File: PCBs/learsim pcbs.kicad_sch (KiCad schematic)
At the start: 54 parts, among them SW1 MHz, SW2 KHz, SW3 2MS1T1B1M2QES-5, U1 ESP32-C6-DEV-KIT-N8, U2 MAX7219, U3 MAX7219

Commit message: Refactor code structure for improved readability and maintainability
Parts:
- removed SW3: 2MS1T1B1M2QES-5, Rotary:SW-TH_2MS1T1B1M2QES-5, symbol Rotary:2MS1T1B1M2QES-5
- added SW4: 2MD1T1B1M2QES-5, Rotary:SW-TH_2MD1T1B1M2QES-5, symbol Rotary:2MD1T1B1M2QES-5
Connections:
- net GND: now also SW4.2
- net LED_12: now also D1.2 (DIN), D5.4 (DOUT); no longer D1.4 (DOUT), D2.2 (DIN)
- net LED_23: now also D1.4 (DOUT), D2.2 (DIN); no longer D2.4 (DOUT), D3.2 (DIN)
- net LED_34: now also D2.4 (DOUT), D3.2 (DIN); no longer D3.4 (DOUT), D4.2 (DIN)
- net LED_45: now also D3.4 (DOUT), D4.2 (DIN); no longer D4.4 (DOUT), D5.2 (DIN)
- net LED_56: now also D4.4 (DOUT); no longer D5.4 (DOUT)
- net LED_DIN: now also D5.2 (DIN); no longer D1.2 (DIN)
- net SW3_A: now also SW4.1; no longer U1.8 (GPIO14)
- net SW3_B: now also SW4.3; no longer U1.15 (EXIO7)
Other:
- moved on the sheet: C6, D1, D2, D3, D4

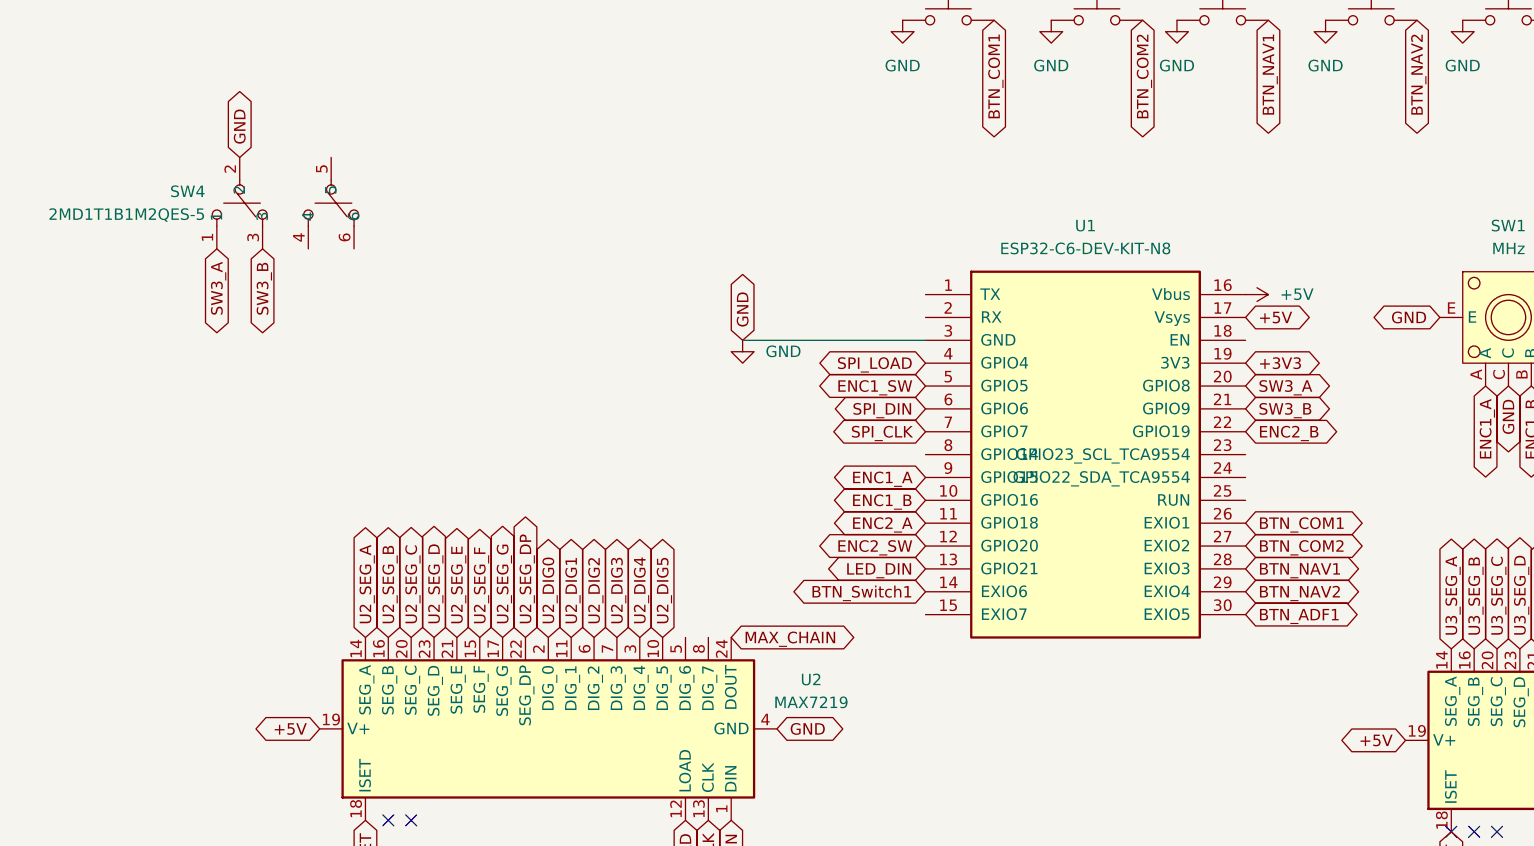
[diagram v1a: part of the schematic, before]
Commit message: Update drill files and job configuration with new timestamps and adjustments
- Updated creation dates in NPTH and PTH drill files to 2026-07-26.
- Adjusted coordinates for several drill points in NPTH file for improved accuracy.
- Modified drill sizes in PTH file, changing T2 from 0.700 to 0.650.
- Added new coordinates in PTH file for additional drill points.
- Updated creation date in job configuration file to 2026-07-26.
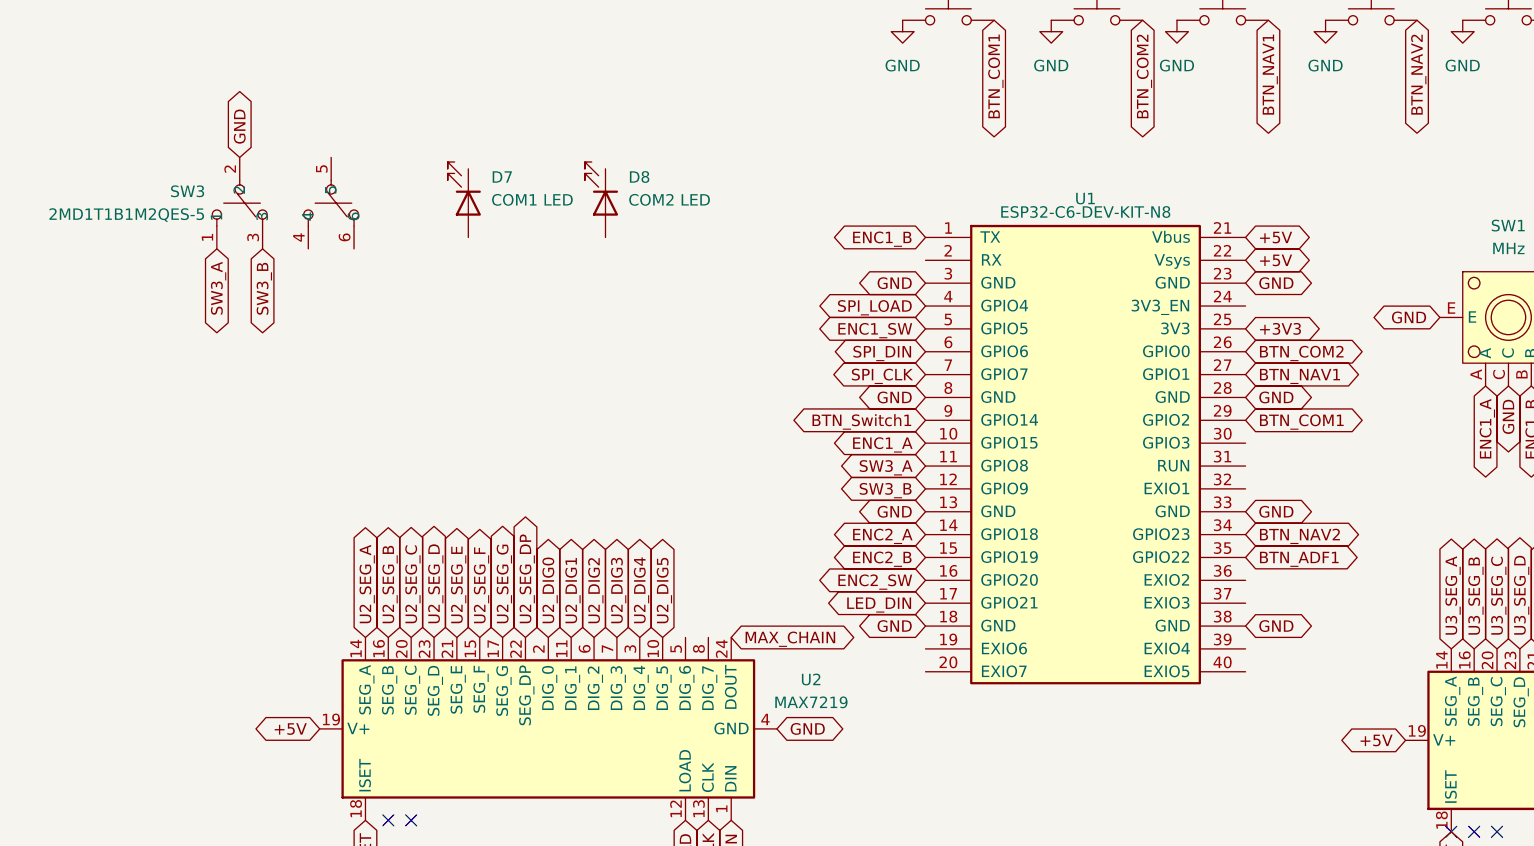
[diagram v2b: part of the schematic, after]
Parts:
- added D7: COM1 LED, LED_THT:LED_D3.0mm, symbol Device:LED
- added D8: COM2 LED, LED_THT:LED_D3.0mm, symbol Device:LED
- renumbered SW4 to SW3
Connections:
- net +3V3: now also U1.25 (3V3); no longer U1.19 (3V3)
- net +5V: now also U1.21 (Vbus), U1.22 (Vsys); no longer U1.16 (Vbus), U1.17 (Vsys)
- net BTN_ADF1: now also U1.35 (GPIO22); no longer U1.30 (EXIO5)
- net BTN_COM1: now also U1.29 (GPIO2); no longer U1.26 (EXIO1)
- net BTN_COM2: now also U1.26 (GPIO0); no longer U1.27 (EXIO2)
- net BTN_NAV1: now also U1.27 (GPIO1); no longer U1.28 (EXIO3)
- net BTN_NAV2: now also U1.34 (GPIO23); no longer U1.29 (EXIO4)
- net BTN_Switch1: now also U1.9 (GPIO14); no longer U1.14 (EXIO6)
- net ENC1_A: now also U1.10 (GPIO15); no longer U1.9 (GPIO15)
- net ENC1_B: now also U1.1 (TX); no longer U1.10 (GPIO16)
- net ENC2_A: now also U1.14 (GPIO18); no longer U1.11 (GPIO18)
- net ENC2_B: now also U1.15 (GPIO19); no longer U1.22 (GPIO19)
- net ENC2_SW: now also U1.16 (GPIO20); no longer U1.12 (GPIO20)
- net GND: now also U1.13 (GND), U1.18 (GND), U1.23 (GND), U1.28 (GND), U1.33 (GND), U1.38 (GND), U1.8 (GND)
- net LED_DIN: now also U1.17 (GPIO21); no longer U1.13 (GPIO21)
- net SW3_A: now also U1.11 (GPIO8); no longer U1.20 (GPIO8)
- net SW3_B: now also U1.12 (GPIO9); no longer U1.21 (GPIO9)

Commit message: Update drill files and job configuration with new creation timestamps and modified drill sizes
- Updated creation timestamps in NPTH and PTH drill files to 2026-07-26T23:00:48.
- Adjusted drill sizes for T4, T5, and T6 in the PTH drill file.
- Added new coordinates in the PTH drill file for improved component placement.
- Updated creation date in the job configuration file to 2026-07-26T23:00:53.
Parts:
- added R17: 150, Resistor_THT:R_Axial_DIN0207_L6.3mm_D2.5mm_P7.62mm_Horizontal, symbol Device:R
- added R18: 470, Resistor_THT:R_Axial_DIN0207_L6.3mm_D2.5mm_P7.62mm_Horizontal, symbol Device:R
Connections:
- net GND: now also D7.1 (K), D8.1 (K)
- net COM2_LED: now reaches U1.2 (RX)
- net COM2_LED: now also R18.2
- net COM1_LED: now reaches U1.30 (GPIO3)
- net COM1_LED: now also R17.2
- net at D8.2 (A): now also R18.1
- net at D7.2 (A): now also R17.1

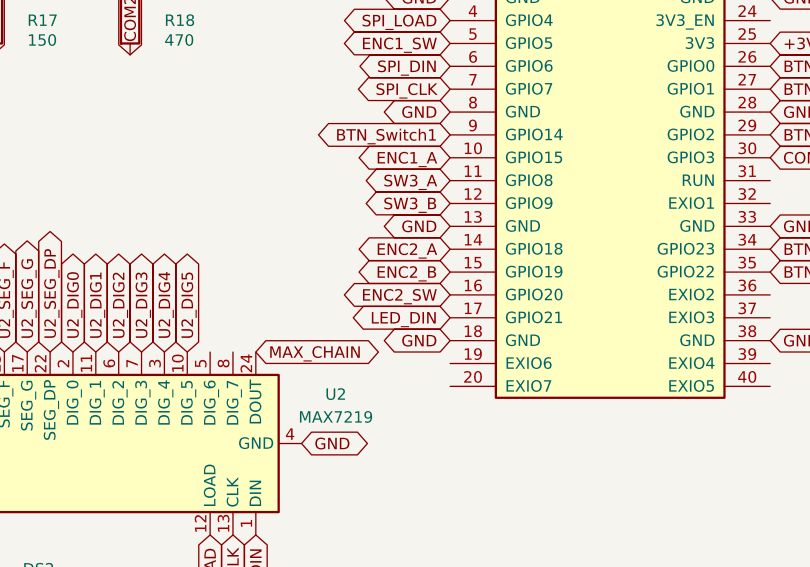
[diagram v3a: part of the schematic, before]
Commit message: Update PCB files with new creation date and modify drill and aperture definitions
- Updated creation date in Gerber files (F_Mask, F_Paste, F_Silkscreen) to 2026-07-27.
- Adjusted aperture definitions in F_Mask for better alignment with design specifications.
- Refined drill files (NPTH and PTH) with updated creation date and corrected tool definitions.
- Enhanced job file with new creation date for consistency across project files.
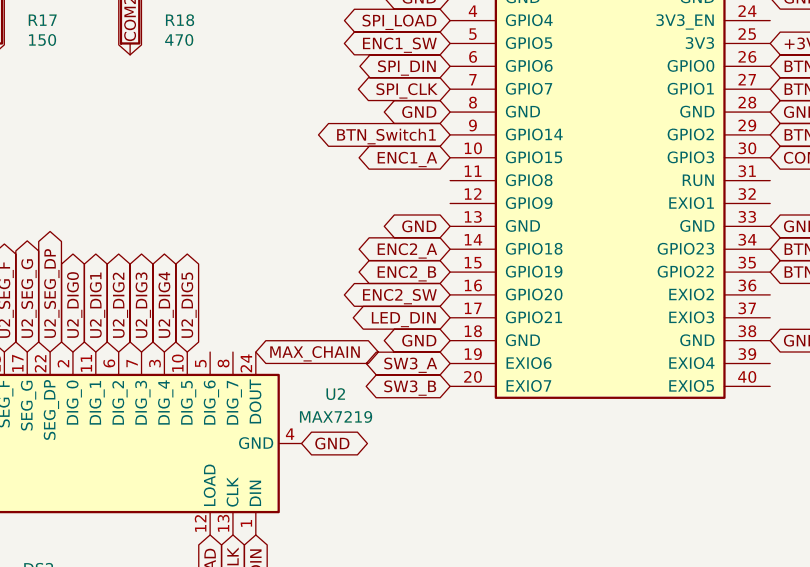
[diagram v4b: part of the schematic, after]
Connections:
- net SW3_A: now also U1.19 (EXIO6); no longer U1.11 (GPIO8)
- net SW3_B: now also U1.20 (EXIO7); no longer U1.12 (GPIO9)
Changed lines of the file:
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@@
 	(global_label "SW3_A"
 		(shape bidirectional)
-		(at 111.76 106.68 180)
-		(fields_autoplaced yes)
-		(effects
-			(font
-				(size 1.27 1.27)
-			)
-			(justify right)
-		)
-		(property "Intersheetrefs" "${INTERSHEET_REFS}"
-			(at 98.8944 106.68 0)
+		(at 111.76 127 180)
+		(fields_autoplaced yes)
+		(effects
+			(font
+				(size 1.27 1.27)
+			)
+			(justify right)
+		)
+		(property "Intersheetrefs" "${INTERSHEET_REFS}"
+			(at 98.8944 127 0)
 			(hide yes)
 			(show_name no)
@@
 	(global_label "SW3_B"
 		(shape bidirectional)
-		(at 111.76 109.22 180)
-		(fields_autoplaced yes)
-		(effects
-			(font
-				(size 1.27 1.27)
-			)
-			(justify right)
-		)
-		(property "Intersheetrefs" "${INTERSHEET_REFS}"
-			(at 98.8944 109.22 0)
-			(hide yes)
-			(show_name no)
+		(at 111.76 129.54 180)
+		(fields_autoplaced yes)
+		(effects
+			(font
+				(size 1.27 1.27)
+			)
+			(justify right)
+		)
+		(property "Intersheetrefs" "${INTERSHEET_REFS}"
+			(at 98.8944 129.54 0)
+			(hide yes)
+			(show_name no)

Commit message: v1.0
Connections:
- net BTN_ADF1: now also U1.37 (EXIO3); no longer U1.35 (GPIO22)
- net BTN_NAV2: now also U1.36 (EXIO2); no longer U1.34 (GPIO23)
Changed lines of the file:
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@@
 	(global_label "BTN_NAV2"
 		(shape bidirectional)
-		(at 147.32 114.3 0)
-		(fields_autoplaced yes)
-		(effects
-			(font
-				(size 1.27 1.27)
-			)
-			(justify left)
-		)
-		(property "Intersheetrefs" "${INTERSHEET_REFS}"
-			(at 160.1856 114.3 0)
+		(at 147.32 119.38 0)
+		(fields_autoplaced yes)
+		(effects
+			(font
+				(size 1.27 1.27)
+			)
+			(justify left)
+		)
+		(property "Intersheetrefs" "${INTERSHEET_REFS}"
+			(at 160.1856 119.38 0)
 			(hide yes)
 			(show_name no)
@@
 	(global_label "BTN_ADF1"
 		(shape bidirectional)
-		(at 147.32 116.84 0)
-		(fields_autoplaced yes)
-		(effects
-			(font
-				(size 1.27 1.27)
-			)
-			(justify left)
-		)
-		(property "Intersheetrefs" "${INTERSHEET_REFS}"
-			(at 160.1856 116.84 0)
+		(at 147.32 121.92 0)
+		(fields_autoplaced yes)
+		(effects
+			(font
+				(size 1.27 1.27)
+			)
+			(justify left)
+		)
+		(property "Intersheetrefs" "${INTERSHEET_REFS}"
+			(at 160.1856 121.92 0)
 			(hide yes)
 			(show_name no)
@@
 	(global_label "MAX_CHAIN"
 		(shape bidirectional)
-		(at 90.17 125.73 0)
-		(fields_autoplaced yes)
-		(effects
-			(font
-				(size 1.27 1.27)
-			)
-			(justify left)
-		)
-		(property "Intersheetrefs" "${INTERSHEET_REFS}"
-			(at 104.608 125.73 0)
-			(hide yes)
-			(show_name no)
+		(at 90.17 125.73 90)
+		(fields_autoplaced yes)
+		(effects
+			(font
+				(size 1.27 1.27)
+			)
+			(justify left)
+		)
+		(property "Intersheetrefs" "${INTERSHEET_REFS}"
+			(at 90.17 111.292 90)
+			(hide yes)
+			(show_name no)
